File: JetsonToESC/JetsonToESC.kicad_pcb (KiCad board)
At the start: 2 copper layers, 70 x 50 mm, 37 parts, among them J1 Conn_01x12, J2 Conn_01x03, J3 Conn_01x02, J4 Screw_Terminal_01x01, J5 Screw_Terminal_01x01, U1 ESP32-C3_SUPERMINI_TH, U2 DS18B20, U3 LMR51420XDDCR, U4 MCP23018x-x-SS, U5 ACS759xCB-100B-PFF

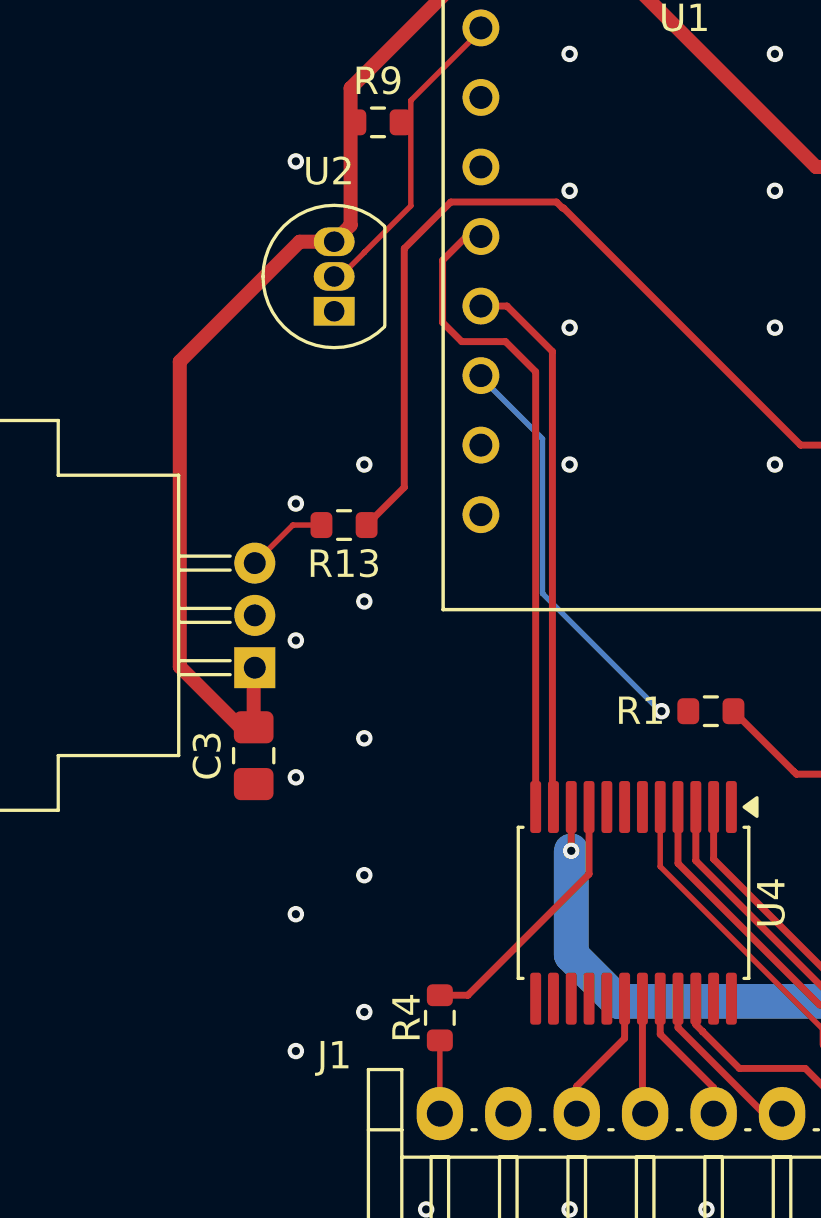
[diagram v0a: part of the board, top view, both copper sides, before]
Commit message: Routed I2C pullups and Reset Added ESP32c3pinout image
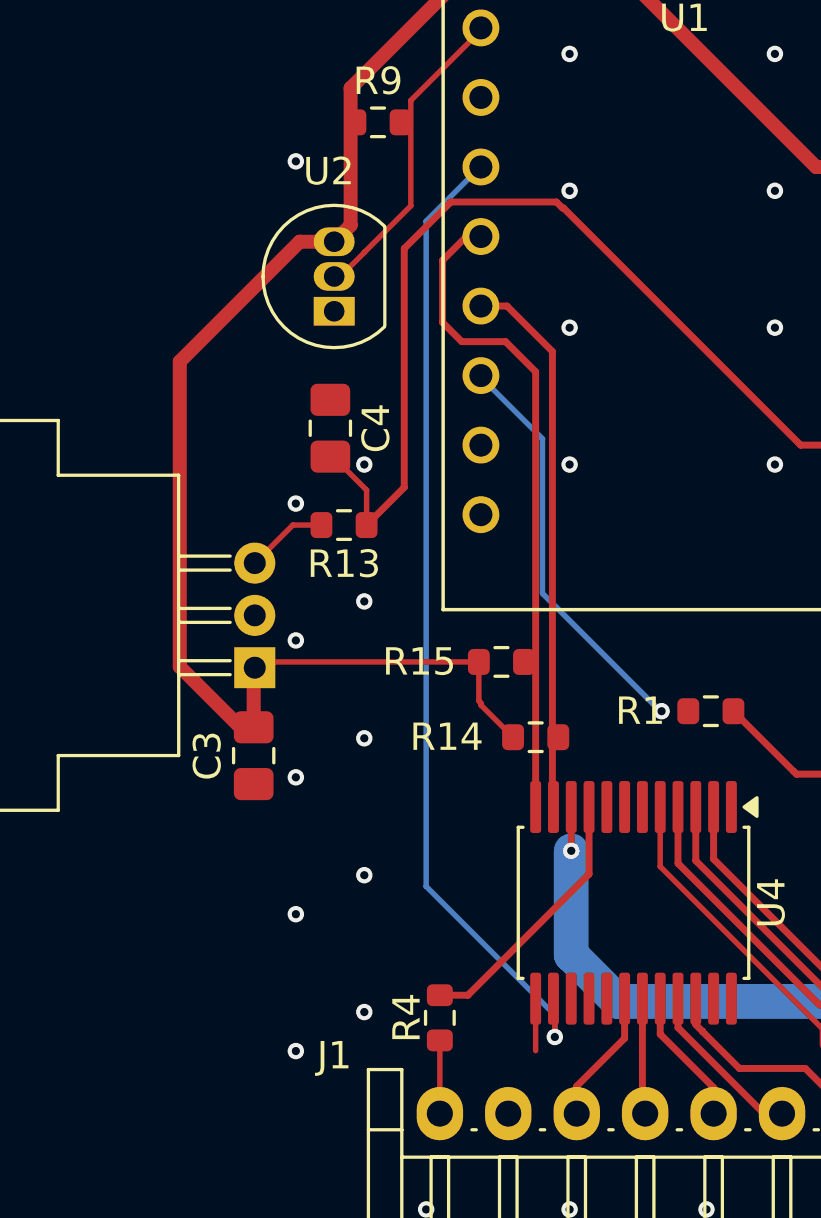
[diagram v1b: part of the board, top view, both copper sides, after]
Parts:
- added C4: 100nF, Capacitor_SMD:C_0805_2012Metric_Pad1.18x1.45mm_HandSolder, F.Cu at (138.5, 97.5)
- added R14: 4K7, Resistor_SMD:R_0603_1608Metric, F.Cu at (146.0, 108.8)
- added R15: 4K7, Resistor_SMD:R_0603_1608Metric, F.Cu at (144.8, 106.0)
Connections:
- U1 pad 7: unconnected-(U1-GPIO7-Pad7) -> I2C_RESET
- U4 pad 13: unconnected-(U4-ADDR-Pad13) -> GND
- U4 pad 14: unconnected-(U4-~{RESET}-Pad14) -> I2C_RESET
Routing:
- net I2C_RESET: track 0.00 -> 36.0 mm, vias 0 -> 1
- net 3V3: track 55.2 -> 66.8 mm
- net CURRENT_SENSE: track 33.1 -> 35.9 mm
- net GND: track 0.00 -> 1.90 mm

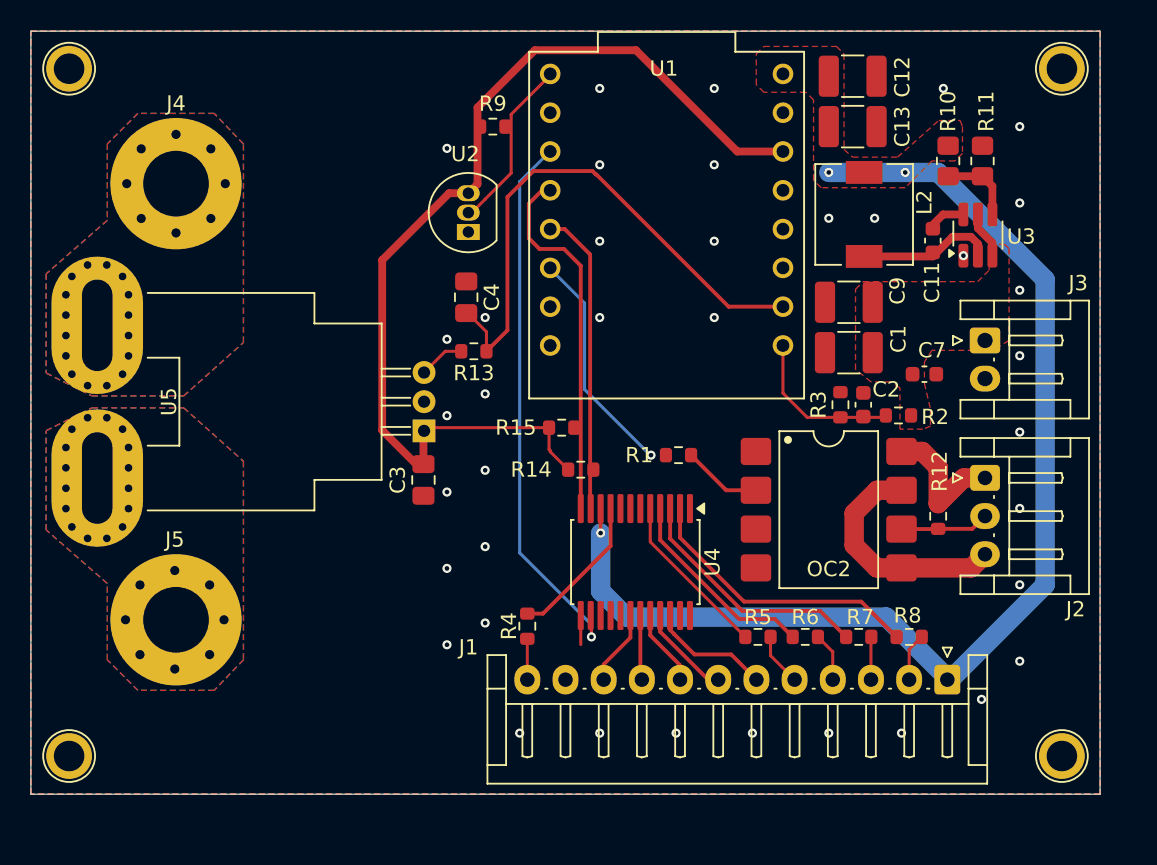
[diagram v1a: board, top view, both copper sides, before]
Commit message: Design almost finished, added vias array for grounding too
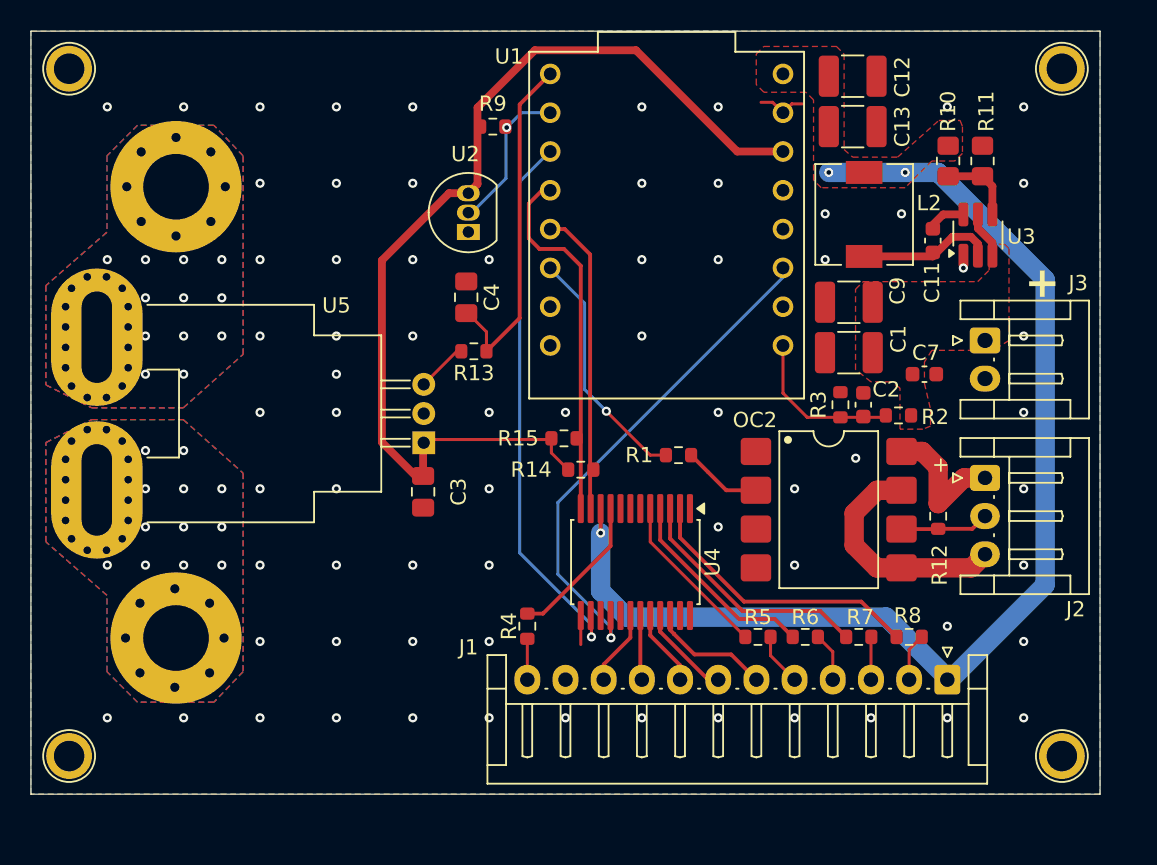
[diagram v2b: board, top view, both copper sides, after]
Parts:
- moved J5 1.19 mm to (119.4, 119.8)
- moved U5 0.78 mm to (135.7, 107.0)
- moved C3 0.78 mm to (135.7, 110.2)
- moved R15 0.72 mm to (144.9, 106.7)
- moved J4 0.20 mm to (119.5, 90.2)
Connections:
- U1 pad 1: CURRENT_SENSE -> unconnected-(U1-GPIO1-Pad1)
- U1 pad 2: unconnected-(U1-GPIO2-Pad2) -> I2C_INT_A
- U1 pad 5: TEMP_SENSE -> CURRENT_SENSE
- U1 pad 6: unconnected-(U1-GPIO6-Pad6) -> TEMP_SENSE
- U4 pad 16: unconnected-(U4-INTA-Pad16) -> I2C_INT_A
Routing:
- net I2C_INT_A: track 0.00 -> 33.3 mm, vias 0 -> 1
- net CURRENT_SENSE: track 35.9 -> 22.8 mm
- net GND: track 1.90 -> 5.77 mm, vias 38 -> 69
- net 3V3: track 66.8 -> 65.3 mm
- net TEMP_SENSE: track 11.4 -> 10.2 mm, vias 0 -> 1
- net PWM: track 15.3 -> 16.2 mm
- net VBAT_OUT: vias 0 -> 12
- net VBAT_IN: vias 0 -> 12
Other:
- board text added: "+"

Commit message: Design almost finished, added vias array for grounding too
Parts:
- added FID1: Fiducial, Fiducial:Fiducial_0.5mm_Mask1.5mm, F.Cu at (117.9, 83.0)
- added FID2: Fiducial, Fiducial:Fiducial_0.5mm_Mask1.5mm, F.Cu at (173.0, 83.0)
- added FID3: Fiducial, Fiducial:Fiducial_0.5mm_Mask1.5mm, F.Cu at (118.0, 127.0)

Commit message: Design and routing done
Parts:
- added C5: 100nF, Capacitor_SMD:C_0603_1608Metric, F.Cu at (136.0, 116.9)
- added C6: 100nF, Capacitor_SMD:C_0603_1608Metric, F.Cu at (149.2, 109.1)
- added MoaBoardsLogo1: ~, Logos:MoaBoards, F.Cu at (128.8, 81.9)
- added R16: 4K7, Resistor_SMD:R_0603_1608Metric, F.Cu at (143.7, 109.2)
- added R17: 4K7, Resistor_SMD:R_0603_1608Metric, F.Cu at (142.0, 105.9)
- added U6: ULN2003, Package_SO:TSSOP-16_4.4x5mm_P0.65mm, F.Cu at (140.2, 113.3)
- R4, R5, R6, R7, R8: value 4K7 -> 120
- U5: value ACS759xCB-100B-PFF -> ACS759ECB-200B-PFF-T
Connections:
- R4 pad 2: Net-(U4-GPB7) -> Net-(U6-O5)
- R5 pad 2: Net-(U4-GPB3) -> Net-(U6-O1)
- R6 pad 2: Net-(U4-GPB2) -> Net-(U6-O2)
- R7 pad 2: Net-(U4-GPB1) -> Net-(U6-O3)
- R8 pad 2: Net-(U4-GPB0) -> Net-(U6-O4)
- U1 pad 0: BATT_LEVEL_SENSE -> unconnected-(U1-GPIO0-Pad0)
- U1 pad 1: unconnected-(U1-GPIO1-Pad1) -> BATT_LEVEL_SENSE
- U1 pad 10: PWM -> I2C_RESET
- U1 pad 7: I2C_RESET -> PWM
- U4 pad 2: Net-(U4-GPB0) -> TEMP
- U4 pad 3: Net-(U4-GPB1) -> BATT_LOW
- U4 pad 4: Net-(U4-GPB2) -> BATT_MED
- U4 pad 5: Net-(U4-GPB3) -> BATT_HI
- U4 pad 6: unconnected-(U4-GPB4-Pad6) -> OVERCURRENT
- U4 pad 9: Net-(U4-GPB7) -> unconnected-(U4-GPB7-Pad9)
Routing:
- net Net-(U6-O4): track 0.00 -> 29.6 mm
- net Net-(U6-O3): track 0.00 -> 25.3 mm
- net 5V: track 76.6 -> 101.4 mm, vias 3 -> 4
- net Net-(U6-O2): track 0.00 -> 20.8 mm
- net Net-(U4-GPB0): track 18.8 -> 0.00 mm
- net TEMP: track 0.00 -> 16.9 mm
- net Net-(U4-GPB1): track 16.2 -> 0.00 mm
- net Net-(U6-O1): track 0.00 -> 15.8 mm
- net BATT_LOW: track 0.00 -> 15.3 mm
- net BATT_MED: track 0.00 -> 13.7 mm
- net Net-(U4-GPB2): track 13.4 -> 0.00 mm
- net BATT_HI: track 0.00 -> 11.9 mm
- net Net-(U4-GPB3): track 11.0 -> 0.00 mm
- net OVERCURRENT: track 0.00 -> 9.88 mm
- net Net-(U4-GPB7): track 9.73 -> 0.00 mm
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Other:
- board text added: "+ Batt through"
- board text added: "-"
- board text added: "1"
- board text added: "12"
- board text added: "IN"
- board text added: "JetsonToESC v1.0 Jan 26'"
- board text added: "OUT"
- board text added: "by RTP"
- board text added: "from Batt"
- board text added: "to ESC"
- board text added: "to Jetson Pannel"

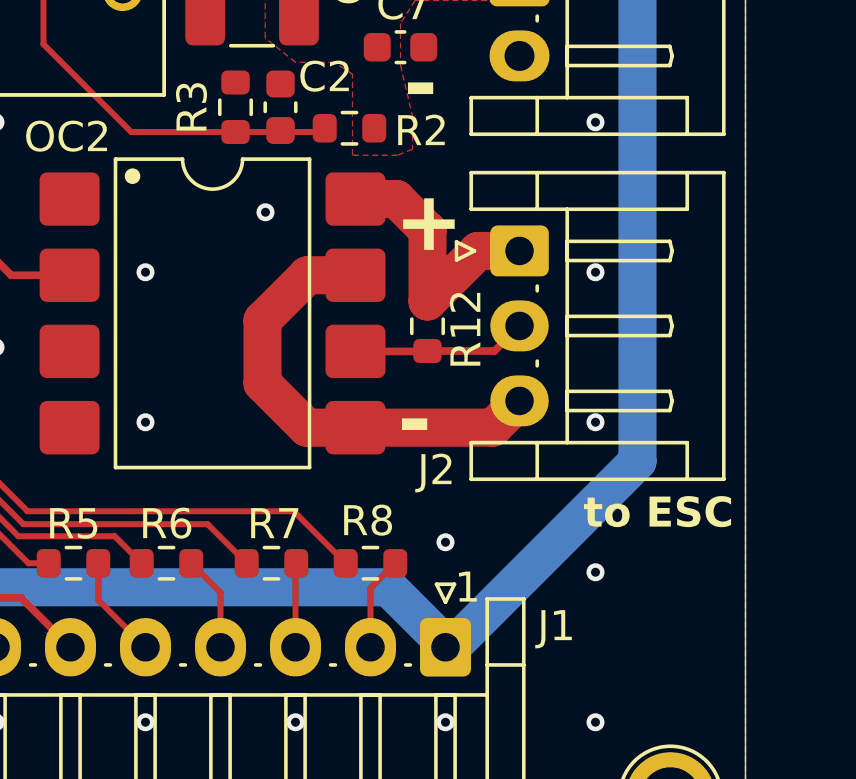
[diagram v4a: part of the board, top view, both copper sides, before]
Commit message: Fix on opto en output, now properly wired
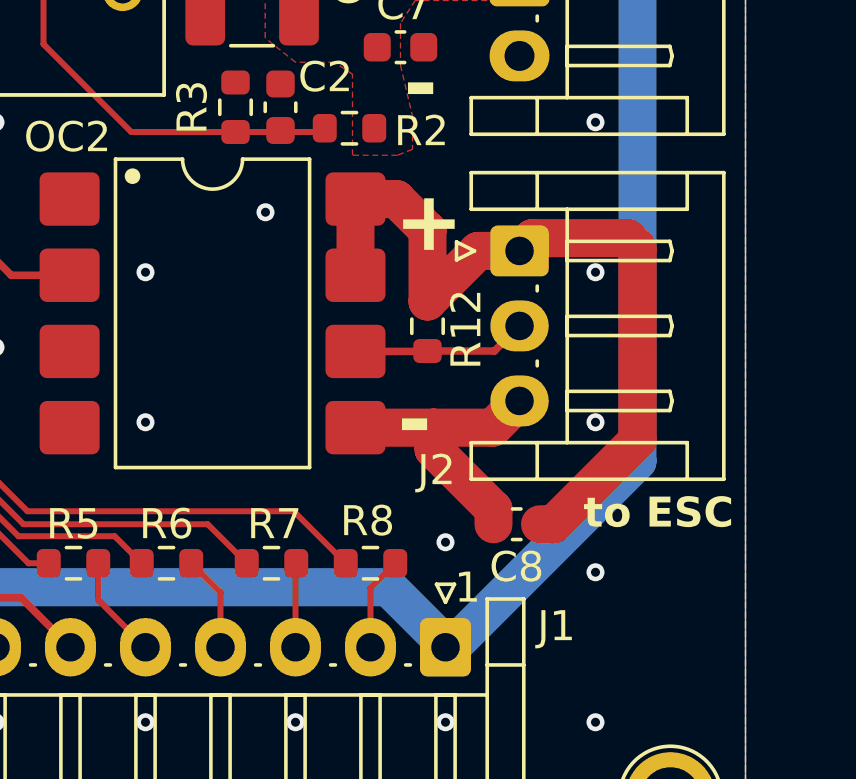
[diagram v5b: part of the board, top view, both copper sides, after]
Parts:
- added C8: 100nF, Capacitor_SMD:C_0603_1608Metric, F.Cu at (172.4, 118.4)
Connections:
- OC2 pad 7: GNDB -> VBEC
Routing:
- net VBEC: track 8.97 -> 26.6 mm
- net GNDB: track 15.4 -> 9.88 mm
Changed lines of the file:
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@@
 		)
 	)
+	(footprint "Capacitor_SMD:C_0603_1608Metric"
+		(layer "F.Cu")
+		(at 172.375 118.4 180)
+		(descr "Capacitor SMD 0603 (1608 Metric), square (rectangular) end terminal, IPC-7351 nominal, (Body size source: IPC-SM-782 page 76, https://www.pcb-3d.com/wordpress/wp-content/uploads/ipc-sm-782a_amendment_1_and_2.pdf), generated with kicad-footprint-generator")
+		(tags "capacitor")
+		(property "Reference" "C8"
+			(at 0 -1.43 0)
+			(layer "F.SilkS")
+			(effects
+				(font
+					(size 1 1)
+					(thickness 0.15)
+				)
+			)
+		)
+		(property "Value" "100nF"
+			(at 0 1.43 0)
+			(layer "F.Fab")
+			(effects
+				(font
+					(size 1 1)
+					(thickness 0.15)
+				)
+			)
+		)
+		(property "Datasheet" "~"
+			(at 0 0 0)
+			(layer "F.Fab")
+			(hide yes)
+			(effects
+				(font
+					(size 1.27 1.27)
+					(thickness 0.15)
+				)
+			)
+		)
+		(property "Description" ""
+			(at 0 0 0)
+			(layer "F.Fab")
+			(hide yes)
+			(effects
+				(font
+					(size 1.27 1.27)
+					(thickness 0.15)
+				)
+			)
+		)
+		(property ki_fp_filters "C_*")
+		(sheetname "/SensnAct/")
+		(sheetfile "sensnact.kicad_sch")
+		(attr smd)
+		(fp_line
+			(start -0.14058 0.51)
+			(end 0.14058 0.51)
+			(stroke
+				(width 0.12)
+				(type solid)
+			)
+			(layer "F.SilkS")
+		)
+		(fp_line
+			(start -0.14058 -0.51)
+			(end 0.14058 -0.51)
+			(stroke
+				(width 0.12)
+				(type solid)
+			)
+			(layer "F.SilkS")
+		)
+		(fp_rect
+			(start -1.48 -0.73)
+			(end 1.48 0.73)
+			(stroke
+				(width 0.05)
+				(type solid)
+			)
+			(fill no)
+			(layer "F.CrtYd")
+		)
+		(fp_rect
+			(start -0.8 -0.4)
+			(end 0.8 0.4)
+			(stroke
+				(width 0.1)
+				(type solid)
+			)
+			(fill no)
+			(layer "F.Fab")
+		)
+		(fp_text user "${REFERENCE}"
+			(at 0 0 0)
+			(layer "F.Fab")
+			(effects
+				(font
+					(size 0.4 0.4)
+					(thickness 0.06)
+				)
+			)
+		)
+		(pad "1" smd roundrect
+			(at -0.775 0 180)
+			(size 0.9 0.95)
+			(layers "F.Cu" "F.Mask" "F.Paste")
+			(roundrect_rratio 0.25)
+			(net 26 "VBEC")
+			(pintype "passive")
+		)
+		(pad "2" smd roundrect
+			(at 0.775 0 180)
+			(size 0.9 0.95)
+			(layers "F.Cu" "F.Mask" "F.Paste")
+			(roundrect_rratio 0.25)
+			(net 25 "GNDB")
+			(pintype "passive")
+		)
+		(embedded_fonts no)
+		(model "${KICAD9_3DMODEL_DIR}/Capacitor_SMD.3dshapes/C_0603_1608Metric.step"
+			(offset
+				(xyz 0 0 0)
+			)
+			(scale
+				(xyz 1 1 1)
+			)
+			(rotate
+				(xyz 0 0 0)
+			)
+		)
+	)
 	(footprint "Package_SO:SSOP-24_5.3x8.2mm_P0.65mm"
 		(layer "F.Cu")
@@
 			(layers "F.Cu" "F.Mask" "F.Paste")
 			(roundrect_rratio 0.1404494382)
-			(net 25 "GNDB")
+			(net 26 "VBEC")
 			(pinfunction "EN")
 			(pintype "input")
@@
 	(segment
 		(start 171.5775 115.18)
-		(end 167 115.18)
-		(width 1.27)
-		(layer "F.Cu")
-		(net 25)
-	)
-	(segment
-		(start 167 115.18)
-		(end 165.38 115.18)
+		(end 169.6 115.18)
 		(width 1.27)
 		(layer "F.Cu")
@@
 	)
 	(segment
-		(start 165.4 110.1)
-		(end 167 110.1)
+		(start 169.6 115.18)
+		(end 169.6 115.9)
 		(width 1.27)
 		(layer "F.Cu")
@@
 	)
 	(segment
-		(start 165.38 115.18)
-		(end 163.9 113.7)
+		(start 172.4675 114.29)
+		(end 171.5775 115.18)
 		(width 1.27)
 		(layer "F.Cu")
@@
 	)
 	(segment
-		(start 172.4675 114.29)
-		(end 171.5775 115.18)
+		(start 169.6 115.18)
+		(end 167 115.18)
 		(width 1.27)
 		(layer "F.Cu")
@@
 	)
 	(segment
-		(start 163.9 111.6)
-		(end 165.4 110.1)
+		(start 169.6 115.9)
+		(end 171.6 117.9)
 		(width 1.27)
 		(layer "F.Cu")
@@
 	)
 	(segment
-		(start 163.9 113.7)
-		(end 163.9 111.6)
+		(start 171.6 117.9)
+		(end 171.6 118.4)
 		(width 1.27)
 		(layer "F.Cu")
@@
 	)
 	(segment
+		(start 173.6 118.4)
+		(end 173.15 118.4)
+		(width 1.27)
+		(layer "F.Cu")
+		(net 26)
+	)
+	(segment
+		(start 176.4 109.2)
+		(end 176.4 115.6)
+		(width 1.27)
+		(layer "F.Cu")
+		(net 26)
+	)
+	(segment
+		(start 167 107.56)
+		(end 167 110.1)
+		(width 1.27)
+		(layer "F.Cu")
+		(net 26)
+	)
+	(segment
+		(start 172.8935 108.864)
+		(end 176.064 108.864)
+		(width 1.27)
+		(layer "F.Cu")
+		(net 26)
+	)
+	(segment
+		(start 172.4675 109.29)
+		(end 172.8935 108.864)
+		(width 1.27)
+		(layer "F.Cu")
+		(net 26)
+	)
+	(segment
 		(start 168.36 107.56)
 		(end 169.4 108.6)
@@
 	)
 	(segment
+		(start 176.064 108.864)
+		(end 176.4 109.2)
+		(width 1.27)
+		(layer "F.Cu")
+		(net 26)
+	)
+	(segment
 		(start 172.4675 109.29)
 		(end 171.085 109.29)
 		(width 1.27)
 		(layer "F.Cu")
+		(net 26)
+	)
+	(segment
+		(start 176.4 115.6)
+		(end 173.6 118.4)
+		(width 1.27)
+		(layer "F.Cu")

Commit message: Updated for v2.0, almost complete
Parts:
- removed C8: 100nF, Capacitor_SMD:C_0603_1608Metric
- removed OC2: 6N137-X007T, PCM_Package_DIP_AKL:SMDIP-8_W9.53mm
- removed R12: 4K7, Resistor_SMD:R_0603_1608Metric
- J2: value Conn_01x03 -> Conn_01x02; footprint Connector_JST:JST_EH_S3B-EH_1x03_P2.50mm_Horizontal -> Connector_JST:JST_EH_S2B-EH_1x02_P2.50mm_Horizontal
- R1: value 220 -> 120
- moved U6 20.3 mm to (160.5, 113.8)
- moved C5 19.7 mm to (155.7, 117.0), turned to 180 degrees
- moved R1 15.2 mm to (166.5, 113.3), turned to 180 degrees
- moved J2 2.58 mm to (172.4, 111.9)
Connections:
- J2 pad 1: VBEC -> ESC_PWM
- J2 pad 2: ESC_PWM -> GNDB
- R1 pad 1: PWM -> ESC_PWM
- R1 pad 2: Net-(OC2-Pad2) -> Net-(U6-O1)
- R4 pad 2: Net-(U6-O5) -> Net-(U6-O7)
- R5 pad 2: Net-(U6-O1) -> Net-(U6-O6)
- R6 pad 2: Net-(U6-O2) -> Net-(U6-O5)
- R7 pad 2: Net-(U6-O3) -> Net-(U6-O4)
- R8 pad 2: Net-(U6-O4) -> Net-(U6-O3)
- U1 pad 3: unconnected-(U1-GPIO3-Pad3) -> CURRENT_SENSE
- U1 pad 5: CURRENT_SENSE -> unconnected-(U1-GPIO5-Pad5)
- U6 pad 1: OVERCURRENT -> PWM
- U6 pad 10: unconnected-(U6-O7-Pad10) -> Net-(U6-O7)
- U6 pad 11: unconnected-(U6-O6-Pad11) -> Net-(U6-O6)
- U6 pad 15: Net-(U6-O2) -> unconnected-(U6-O2-Pad15)
- U6 pad 2: BATT_HI -> unconnected-(U6-I2-Pad2)
- U6 pad 3: BATT_MED -> OVERCURRENT
- U6 pad 4: BATT_LOW -> BATT_HI
- U6 pad 5: TEMP -> BATT_MED
- U6 pad 6: unconnected-(U6-I6-Pad6) -> BATT_LOW
- U6 pad 7: unconnected-(U6-I7-Pad7) -> TEMP
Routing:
- net VBEC: track 26.6 -> 0.00 mm
- net Net-(U6-O4): track 29.6 -> 4.34 mm
- net 5V: track 101.4 -> 77.9 mm
- net Net-(U6-O2): track 20.8 -> 0.00 mm
- net Net-(U6-O7): track 0.00 -> 18.9 mm
- net Net-(U6-O3): track 25.3 -> 7.14 mm
- net Net-(U6-O1): track 15.8 -> 4.88 mm
- net CURRENT_SENSE: track 22.8 -> 32.7 mm
- net GNDB: track 9.88 -> 0.00 mm
- net TEMP: track 16.9 -> 8.65 mm
- net PWM: track 24.1 -> 31.2 mm
- net OVERCURRENT: track 9.88 -> 15.3 mm
- net Net-(OC2-Pad2): track 5.20 -> 0.00 mm
- net BATT_LOW: track 15.3 -> 10.3 mm
- net Net-(U6-O6): track 0.00 -> 4.92 mm
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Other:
- board text added: "JetsonToESC v2.0 Mar 26'"
- board text removed: "JetsonToESC v1.0 Jan 26'"
